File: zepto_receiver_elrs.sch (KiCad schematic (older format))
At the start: 44 parts, among them J1 u.fl, SW1 SW_Push, U1 STM32WLE5JBI6, U2 NCP160, U3 BGS12PL6E6327XTSA1, U4 0900FM15D0039, U5 ECS-TXO-25CSMV-320-AM-TR

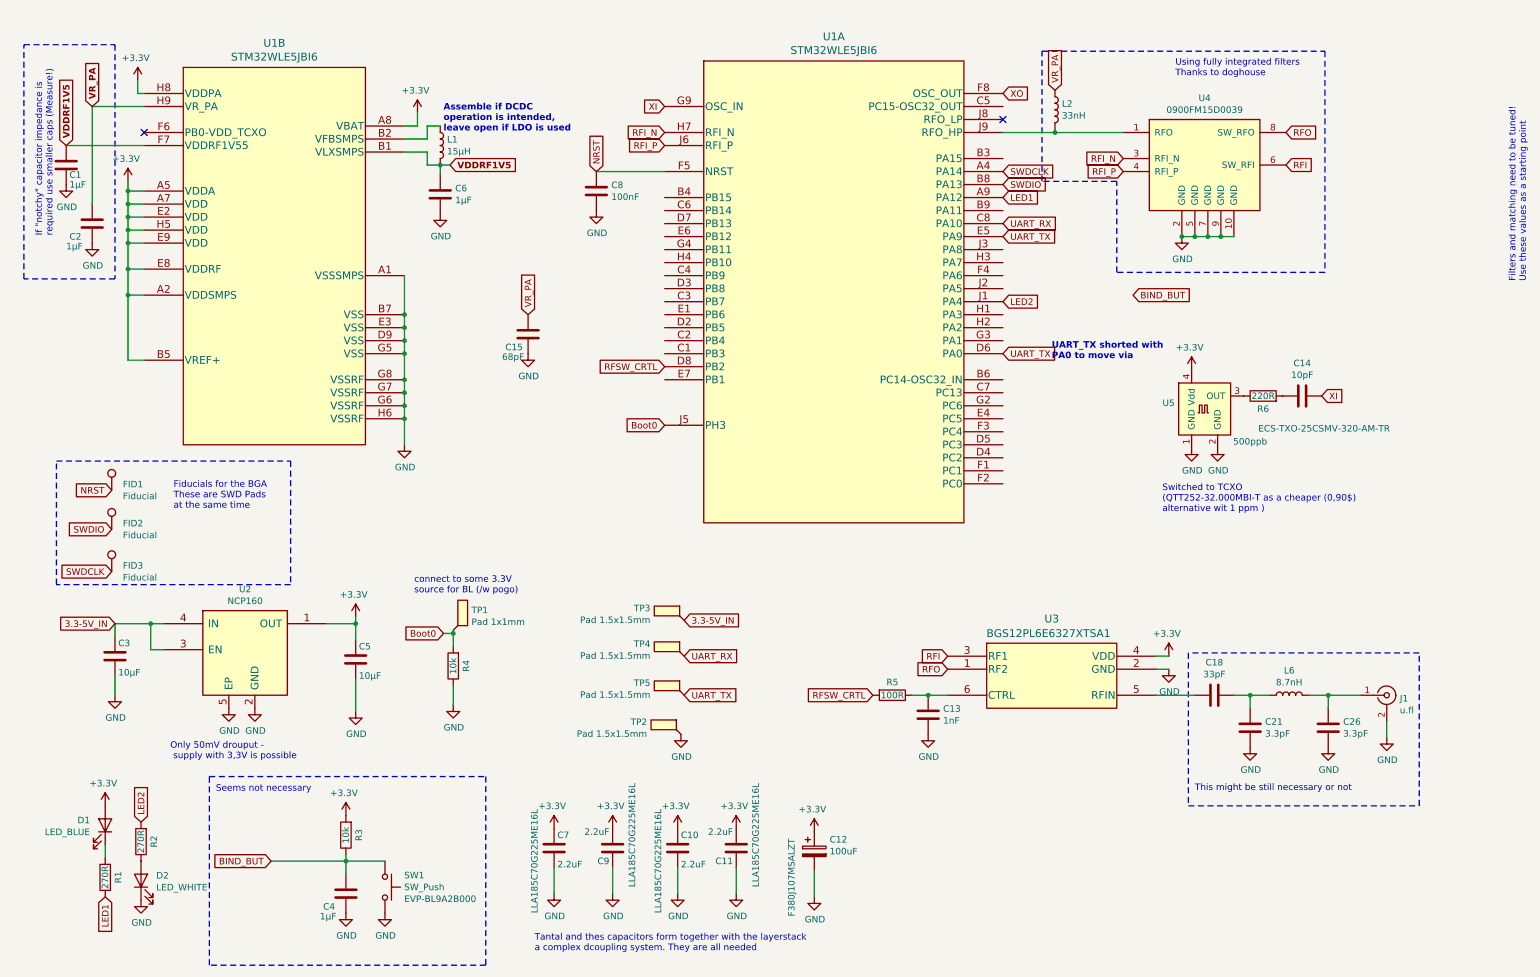
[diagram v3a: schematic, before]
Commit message: Created panels, changed sideplating, added a few comments
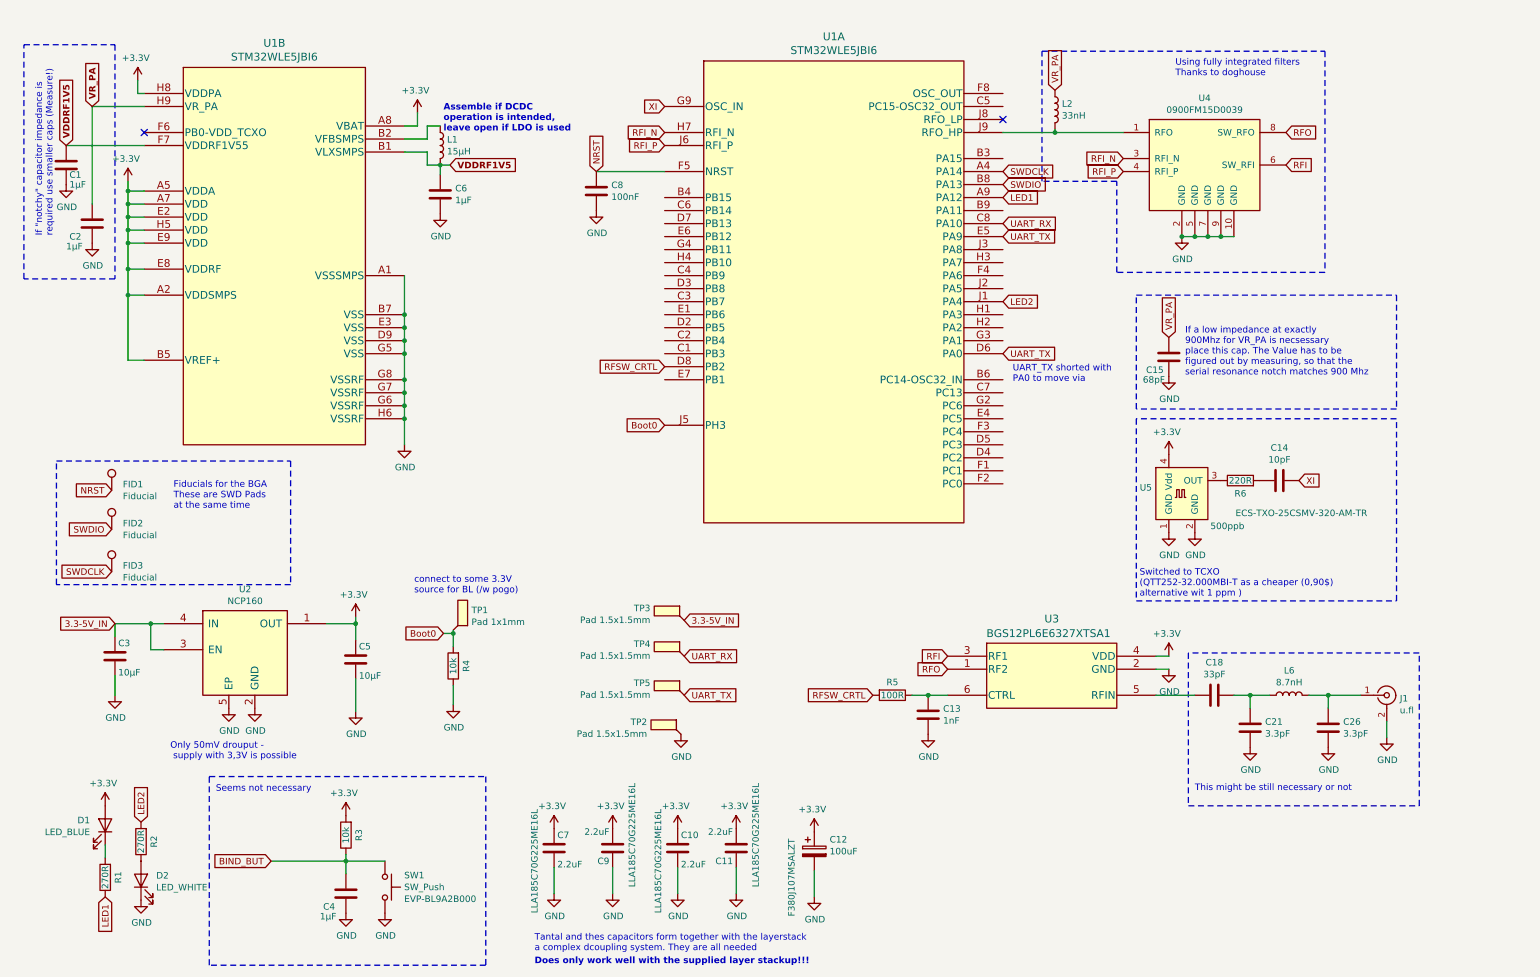
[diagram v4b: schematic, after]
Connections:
- net XO: no longer names the net of U1.F8 (OSC_OUT)
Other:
- note added: "Does only work well with the supplied layer stackup!!!\n"
- note added: "If a low impedance at exactly \n900Mhz for VR_PA is necsessary \nplace this cap. The Value has to be \nfigured out by measuring, so that the \nserial resonance notch matches 900 Mhz"
- note added: "Tantal and thes capacitors form together with the layerstack\na complex dcoupling system. They are all needed\n"
- note removed: "Filters and matching need to be tuned!\nUse these values as a starting point\n"
- note removed: "Tantal and thes capacitors form together with the layerstack\na complex dcoupling system. They are all needed"
- moved on the sheet: C14, C15, R6, U5
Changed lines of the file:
@@
 EESchema Schematic File Version 4
+LIBS:zepto_receiver_elrs-cache
 EELAYER 30 0
 EELAYER END
@@
 Text GLabel 5400 1150 0    50   Input ~ 0
 XI
-Text GLabel 8000 1050 2    50   Input ~ 0
-XO
 $Comp
 L power:GND #PWR02
@@
 Text GLabel 5400 3150 0    50   Input ~ 0
 RFSW_CRTL
-Text Notes 12025 2500 1    50   ~ 0
-Filters and matching need to be tuned!\nUse these values as a starting point\n
 Text Notes 9475 6500 0    50   ~ 0
 This might be still necessary or not\n\n
@@
 	1    0    0    -1
 $EndComp
-Text GLabel 9000 2600 2    50   Input ~ 0
-BIND_BUT
 $Comp
 L power:+3.3V #PWR09
@@
 L sch_comp:ECS-TXO-25CSMV U5
 U 1 1 604C7152
-P 9550 3475
-F 0 "U5" H 9320 3521 50  0000 R CNN
-F 1 "ECS-TXO-25CSMV-320-AM-TR" H 10975 3325 50  0000 R CNN
-F 2 "ftprnts:ECS-TXO-25CSMV-320-AM-TR_reduced_pads" H 10250 3025 50  0001 C CNN
-F 3 "" H 10250 3025 50  0001 C CNN
-F 4 "500ppb" H 9900 3225 50  0000 C CNN "Tolerance"
-F 5 "1,64" H 9550 3475 50  0001 C CNN "BomCos@10k"
-	1    9550 3475
+P 9375 4125
+F 0 "U5" H 9145 4171 50  0000 R CNN
+F 1 "ECS-TXO-25CSMV-320-AM-TR" H 10800 3975 50  0000 R CNN
+F 2 "ftprnts:ECS-TXO-25CSMV-320-AM-TR_reduced_pads" H 10075 3675 50  0001 C CNN
+F 3 "" H 10075 3675 50  0001 C CNN
+F 4 "500ppb" H 9725 3875 50  0000 C CNN "Tolerance"
+F 5 "1,64" H 9375 4125 50  0001 C CNN "BomCos@10k"
+	1    9375 4125
 	1    0    0    -1
 $EndComp
@@
 L Device:C C14
 U 1 1 604C890B
-P 10300 3375
-F 0 "C14" V 10552 3375 50  0000 C CNN
-F 1 "10pF" V 10461 3375 50  0000 C CNN
-F 2 "ftprnts:C_0201_0603Metric_dense" H 10338 3225 50  0001 C CNN
-F 3 "~" H 10300 3375 50  0001 C CNN
-F 4 "0,05" H 10300 3375 50  0001 C CNN "BomCos@10k"
-	1    10300 3375
+P 10125 4025
+F 0 "C14" V 10377 4025 50  0000 C CNN
+F 1 "10pF" V 10286 4025 50  0000 C CNN
+F 2 "ftprnts:C_0201_0603Metric_dense" H 10163 3875 50  0001 C CNN
+F 3 "~" H 10125 4025 50  0001 C CNN
+F 4 "0,05" H 10125 4025 50  0001 C CNN "BomCos@10k"
+	1    10125 4025
 	0    -1   -1   0
 $EndComp
@@
 L Device:R R6
 U 1 1 604C9485
-P 10000 3375
-F 0 "R6" V 9900 3375 50  0000 C CNN
-F 1 "220R" V 10000 3375 50  0000 C CNN
-F 2 "ftprnts:R_0201_0603Metric_dense" V 9930 3375 50  0001 C CNN
-F 3 "~" H 10000 3375 50  0001 C CNN
-F 4 "0,003" H 10000 3375 50  0001 C CNN "BomCos@10k"
-F 5 "RC0201FR-07270RL" H 10000 3375 50  0001 C CNN "Type"
-	1    10000 3375
+P 9825 4025
+F 0 "R6" V 9725 4025 50  0000 C CNN
+F 1 "220R" V 9825 4025 50  0000 C CNN
+F 2 "ftprnts:R_0201_0603Metric_dense" V 9755 4025 50  0001 C CNN
+F 3 "~" H 9825 4025 50  0001 C CNN
+F 4 "0,003" H 9825 4025 50  0001 C CNN "BomCos@10k"
+F 5 "RC0201FR-07270RL" H 9825 4025 50  0001 C CNN "Type"
+	1    9825 4025
 	0    -1   -1   0
 $EndComp
-Text GLabel 10450 3375 2    50   Input ~ 0
+Text GLabel 10275 4025 2    50   Input ~ 0
 XI
 $Comp
 L power:GND #PWR0103
 U 1 1 604CCBA0
-P 9450 3775
-F 0 "#PWR0103" H 9450 3525 50  0001 C CNN
-F 1 "GND" H 9455 3602 50  0000 C CNN
-F 2 "" H 9450 3775 50  0001 C CNN
-F 3 "" H 9450 3775 50  0001 C CNN
-	1    9450 3775
+P 9275 4425
+F 0 "#PWR0103" H 9275 4175 50  0001 C CNN
+F 1 "GND" H 9280 4252 50  0000 C CNN
+F 2 "" H 9275 4425 50  0001 C CNN
+F 3 "" H 9275 4425 50  0001 C CNN
+	1    9275 4425
 	1    0    0    -1
 $EndComp
@@
 L power:GND #PWR0104
 U 1 1 604CD2CB
-P 9650 3775
-F 0 "#PWR0104" H 9650 3525 50  0001 C CNN
-F 1 "GND" H 9655 3602 50  0000 C CNN
-F 2 "" H 9650 3775 50  0001 C CNN
-F 3 "" H 9650 3775 50  0001 C CNN
-	1    9650 3775
+P 9475 4425
+F 0 "#PWR0104" H 9475 4175 50  0001 C CNN
+F 1 "GND" H 9480 4252 50  0000 C CNN
+F 2 "" H 9475 4425 50  0001 C CNN
+F 3 "" H 9475 4425 50  0001 C CNN
+	1    9475 4425
 	1    0    0    -1
 $EndComp
@@
 L power:+3.3V #PWR0105
 U 1 1 604CD48E
-P 9450 3175
-F 0 "#PWR0105" H 9450 3025 50  0001 C CNN
-F 1 "+3.3V" H 9465 3348 50  0000 C CNN
-F 2 "" H 9450 3175 50  0001 C CNN
-F 3 "" H 9450 3175 50  0001 C CNN
-	1    9450 3175
+P 9275 3825
+F 0 "#PWR0105" H 9275 3675 50  0001 C CNN
+F 1 "+3.3V" H 9290 3998 50  0000 C CNN
+F 2 "" H 9275 3825 50  0001 C CNN
+F 3 "" H 9275 3825 50  0001 C CNN
+	1    9275 3825
 	-1   0    0    -1
 $EndComp
@@
 Text Notes 9325 925  0    50   ~ 0
 Using fully integrated filters\nThanks to doghouse
-Text Notes 9225 4275 0    50   ~ 0
+Text Notes 9050 4925 0    50   ~ 0
 Switched to TCXO\n(QTT252-32.000MBI-T as a cheaper (0,90$)\nalternative wit 1 ppm )
 Wire Notes Line
@@
 Seems not necessary
 Text Notes 4400 7650 0    50   ~ 0
-Tantal and thes capacitors form together with the layerstack\na complex dcoupling system. They are all needed
+Tantal and thes capacitors form together with the layerstack\na complex dcoupling system. They are all needed\n
 Text GLabel 7575 5475 0    50   Input ~ 0
 RFO
@@
 Text GLabel 8000 3050 2    50   Input ~ 0
 UART_TX
-Text Notes 8375 3100 0    50   ~ 10
+Text Notes 8075 3275 0    50   ~ 0
 UART_TX shorted with\nPA0 to move via
 Text Notes 1625 4250 0    50   ~ 0
@@
 L Device:C C15
 U 1 1 6057CEF1
-P 4350 2900
-F 0 "C15" H 4175 2800 50  0000 L CNN
-F 1 "68pF" H 4150 2725 50  0000 L CNN
-F 2 "ftprnts:C_0201_0603Metric_dense" H 4388 2750 50  0001 C CNN
-F 3 "~" H 4350 2900 50  0001 C CNN
-F 4 "0,014" H 4350 2900 50  0001 C CNN "BomCos@10k"
-F 5 "GRM033C80J105ME05J" H 4350 2900 50  0001 C CNN "Type"
-	1    4350 2900
-	1    0    0    -1
-$EndComp
-Text GLabel 4350 2750 1    50   Input ~ 0
+P 9275 3075
+F 0 "C15" H 9100 2975 50  0000 L CNN
+F 1 "68pF" H 9075 2900 50  0000 L CNN
+F 2 "ftprnts:C_0201_0603Metric_dense" H 9313 2925 50  0001 C CNN
+F 3 "~" H 9275 3075 50  0001 C CNN
+F 4 "0,014" H 9275 3075 50  0001 C CNN "BomCos@10k"
+F 5 "GRM033C80J105ME05J" H 9275 3075 50  0001 C CNN "Type"
+	1    9275 3075
+	1    0    0    -1
+$EndComp
+Text GLabel 9275 2925 1    50   Input ~ 0
 VR_PA
 $Comp
 L power:GND #PWR0106
 U 1 1 6058AA62
-P 4350 3050
-F 0 "#PWR0106" H 4350 2800 50  0001 C CNN
-F 1 "GND" H 4355 2877 50  0000 C CNN
-F 2 "" H 4350 3050 50  0001 C CNN
-F 3 "" H 4350 3050 50  0001 C CNN
-	1    4350 3050
-	1    0    0    -1
-$EndComp
+P 9275 3225
+F 0 "#PWR0106" H 9275 2975 50  0001 C CNN
+F 1 "GND" H 9280 3052 50  0000 C CNN
+F 2 "" H 9275 3225 50  0001 C CNN
+F 3 "" H 9275 3225 50  0001 C CNN
+	1    9275 3225
+	1    0    0    -1
+$EndComp
+Text Notes 4400 7750 0    50   ~ 10
+Does only work well with the supplied layer stackup!!!\n
+Text Notes 9400 3225 0    50   ~ 0
+If a low impedance at exactly \n900Mhz for VR_PA is necsessary \nplace this cap. The Value has to be \nfigured out by measuring, so that the \nserial resonance notch matches 900 Mhz
+Wire Notes Line
+	9025 2600 11025 2600
+Wire Notes Line
+	11025 2600 11025 3475
+Wire Notes Line
+	11025 3475 9025 3475
+Wire Notes Line
+	9025 3475 9025 2600
+Wire Notes Line
+	9025 3550 9025 4950
+Wire Notes Line
+	9025 4950 11025 4950
+Wire Notes Line
+	11025 4950 11025 3550
+Wire Notes Line
+	11025 3550 9025 3550
 $EndSCHEMATC
